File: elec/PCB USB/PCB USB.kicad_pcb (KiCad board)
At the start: 4 copper layers, 91 x 38 mm, 86 parts, among them J201 USB_C_PICO, J402 USB_C_Receptacle_USB2.0_14P, J403 USB_A, J404 USB_C_Receptacle_USB2.0_14P, J405 USB_A, J501 Conn_I2C_Écran, P1 USB_C_Plug_USB2.0, Q301 AO3401A, Q401 AO3401A, SW201 SW_BOOTSEL, SW202 SW_RESET, SW501 RotaryEncoder_Switch, U201 SRV05-4, U202 RP2350B-QFN80, U203 W25Q128JVPIQ, U301 AP7361C-33E, U401 SRV05-4, Y201 CM4012M00012001, Y401 12MHz

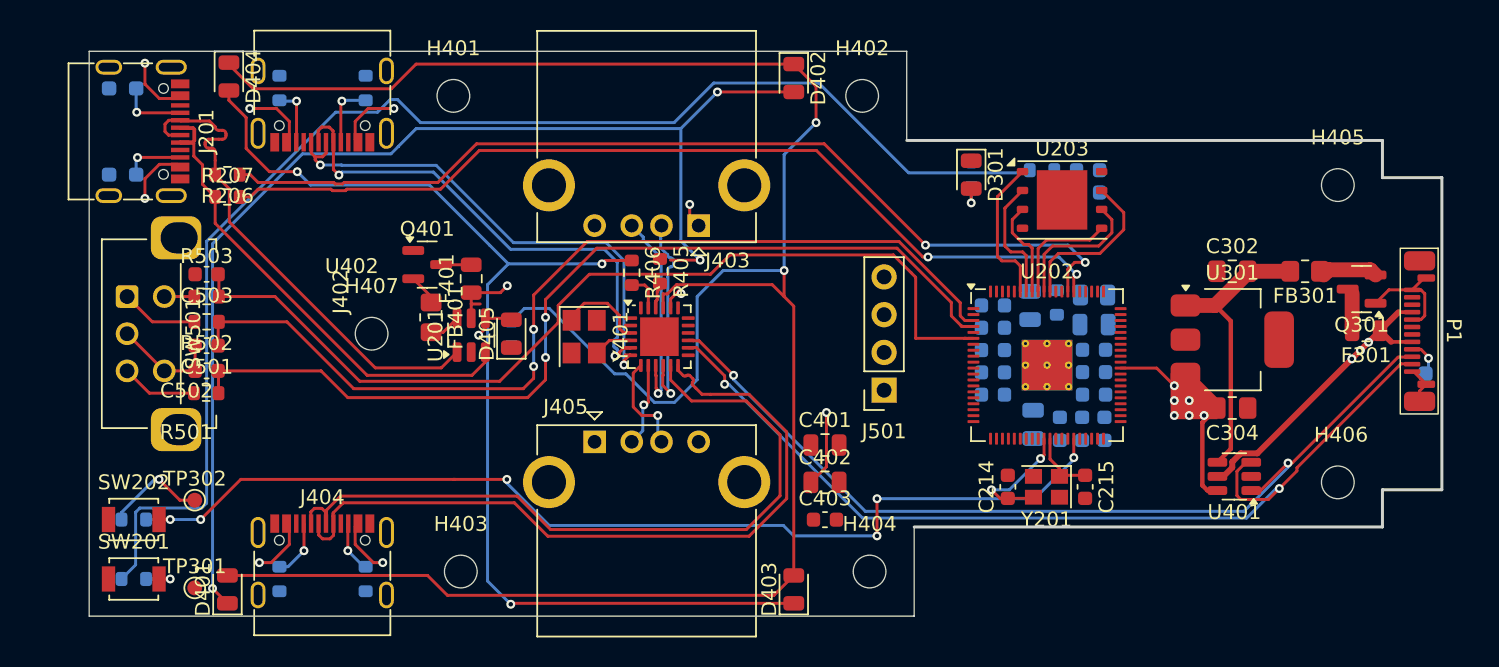
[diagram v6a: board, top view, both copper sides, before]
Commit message: push finalisation pcb et silkscreen
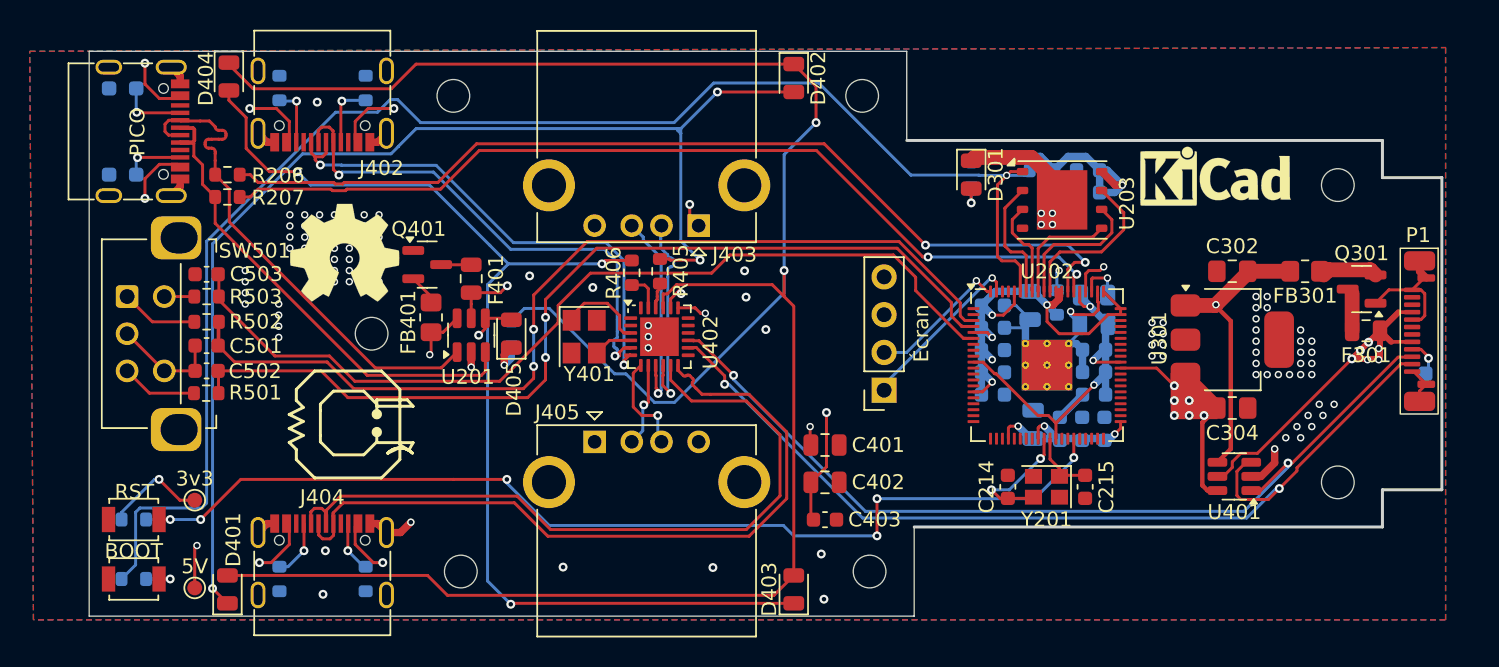
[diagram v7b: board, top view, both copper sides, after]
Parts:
- added REF**: OSHW-Symbol_13.4x12mm_SilkScreen, Symbol:OSHW-Symbol_13.4x12mm_SilkScreen, F.Cu at (101.7, 92.6)
- added REF**: KiCad-Logo_8mm_SilkScreen, Symbol:KiCad-Logo_8mm_SilkScreen, F.Cu at (160.3, 87.4)
- renumbered TP302 to 3v3, TP301 to 5V, SW201 to BOOT, J201 to PICO, SW202 to RST, J501 to Écran
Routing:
- net +5V: track 21.6 -> 117.8 mm, vias 0 -> 5
- net +3V3: track 113.6 -> 178.9 mm, vias 10 -> 19
- net GND: track 17.5 -> 57.3 mm, vias 0 -> 112
- net +1V1: track 0.00 -> 25.3 mm, vias 0 -> 3
- net /MCU/GPIO2: track 0.00 -> 11.7 mm, vias 0 -> 1
- net /MCU/GPIO3: track 0.00 -> 9.55 mm, vias 0 -> 1
- net Net-(U202-VREG_VIN): track 0.00 -> 7.84 mm, vias 0 -> 2
- net VBUS: track 248.9 -> 252.0 mm, vias 11 -> 14
- net Net-(U202-VREG_LX): track 0.00 -> 3.09 mm, vias 0 -> 1
- net Net-(D405-K): track 0.00 -> 2.85 mm, vias 0 -> 1
- net Net-(D401-A): track 152.9 -> 150.5 mm
- net /MCU/GPIO8: track 63.7 -> 61.9 mm
- net Net-(D401-K): track 79.4 -> 80.6 mm
- net /MCU/GPIO6: track 64.3 -> 65.3 mm
- net /MCU/~{QSPI_CS_{0}}: track 101.1 -> 101.7 mm, vias 0 -> 1
- added copper zone on B.Cu, net GND
- added copper zone on F.Cu, net GND
- added copper zone on In1.Cu, net GND
- added copper zone on F.Cu, net VBUS
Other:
- board text added: "Compétition C3I H25 Pomodoro + HUB USB"
- board text added: "PCB créé par: Charles-Ariel Dion & Jacob Turcotte"
